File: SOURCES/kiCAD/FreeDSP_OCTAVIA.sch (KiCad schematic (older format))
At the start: 163 parts, among them IC1 TPS5430DDA, J13 Conn_01x05, J2 DC7.5V-9V IN, J4 Header_01x06, J7 Header_01x04, J8 Header_01x04, P1 Conn_02x20_Odd_Even, Q1 AO3401A, Q2 MMBT5401, Q3 2N7002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

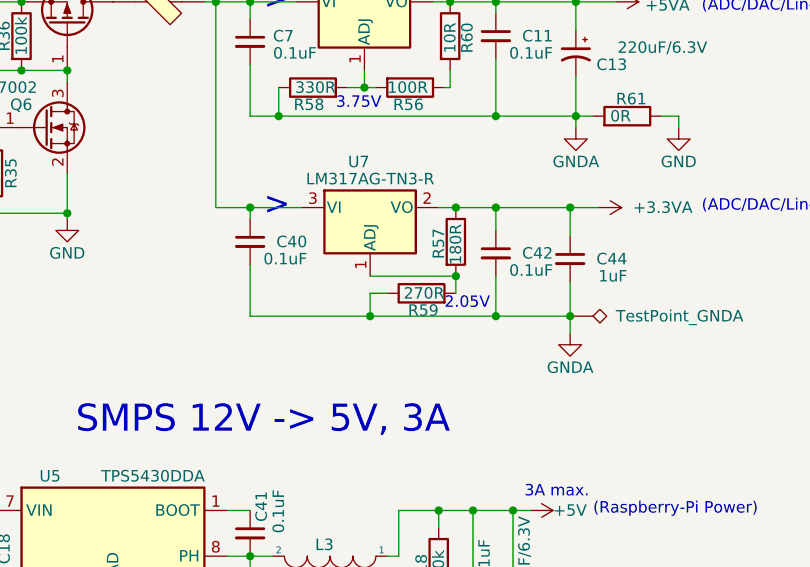
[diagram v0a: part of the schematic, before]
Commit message: Fixed R57, R59 value errors
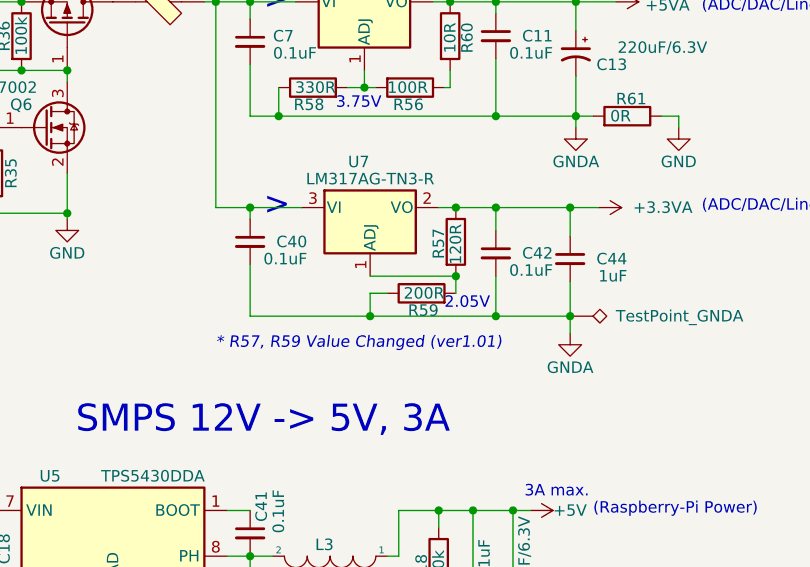
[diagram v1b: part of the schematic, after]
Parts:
- R57: value 180R -> 120R
- R59: value 270R -> 200R; JLPCB# C22962 -> C8218
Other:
- note added: "* R57, R59 Value Changed (ver1.01)"
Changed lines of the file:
@@
 Sheet 1 3
 Title "FreeDSP OVTAVIA Main Board"
-Date "2023-09-30"
-Rev "1.00"
+Date "2023-10-07"
+Rev "1.01"
 Comp ""
 Comment1 ""
@@
 P 10850 4450
 F 0 "R59" V 10775 4375 50  0000 L CNN
-F 1 "270R" V 10850 4350 50  0000 L CNN
+F 1 "200R" V 10850 4350 50  0000 L CNN
 F 2 "Resistor_SMD:R_0603_1608Metric" V 10780 4450 50  0001 C CNN
 F 3 "~" H 10850 4450 50  0001 C CNN
-F 4 "C22962" H 10850 4450 50  0001 C CNN "JLPCB#"
+F 4 "C8218" H 10850 4450 50  0001 C CNN "JLPCB#"
 	1    10850 4450
 	0    -1   -1   0
@@
 P 11000 4225
 F 0 "R57" V 10925 4150 50  0000 L CNN
-F 1 "180R" V 11000 4125 50  0000 L CNN
+F 1 "120R" V 11000 4125 50  0000 L CNN
 F 2 "Resistor_SMD:R_0603_1608Metric" V 10930 4225 50  0001 C CNN
 F 3 "~" H 11000 4225 50  0001 C CNN
@@
 Wire Wire Line
 	11975 3675 11900 3675
+Text Notes 9950 4700 0    50   Italic 0
+* R57, R59 Value Changed (ver1.01)
 $EndSCHEMATC

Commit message: Fixed ACM9070F Land Patterns.
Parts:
- FL1: footprint MyLibrary:ACM9070 -> MyLibrary:ACM9070F
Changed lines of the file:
@@
 Sheet 1 3
 Title "FreeDSP OVTAVIA Main Board"
-Date "2023-10-07"
-Rev "1.01"
+Date "2023-11-29"
+Rev "1.02"
 Comp ""
 Comment1 ""
@@
 F 0 "FL1" H 2650 1575 50  0000 C CNN
 F 1 "ACM9070" H 2725 1500 50  0000 C CNN
-F 2 "MyLibrary:ACM9070" V 2425 1365 50  0001 C CNN
+F 2 "MyLibrary:ACM9070F" V 2425 1365 50  0001 C CNN
 F 3 "~" V 2425 1365 50  0000 C CNN
 F 4 "C908578" H 2425 1325 50  0001 C CNN "JLPCB#"

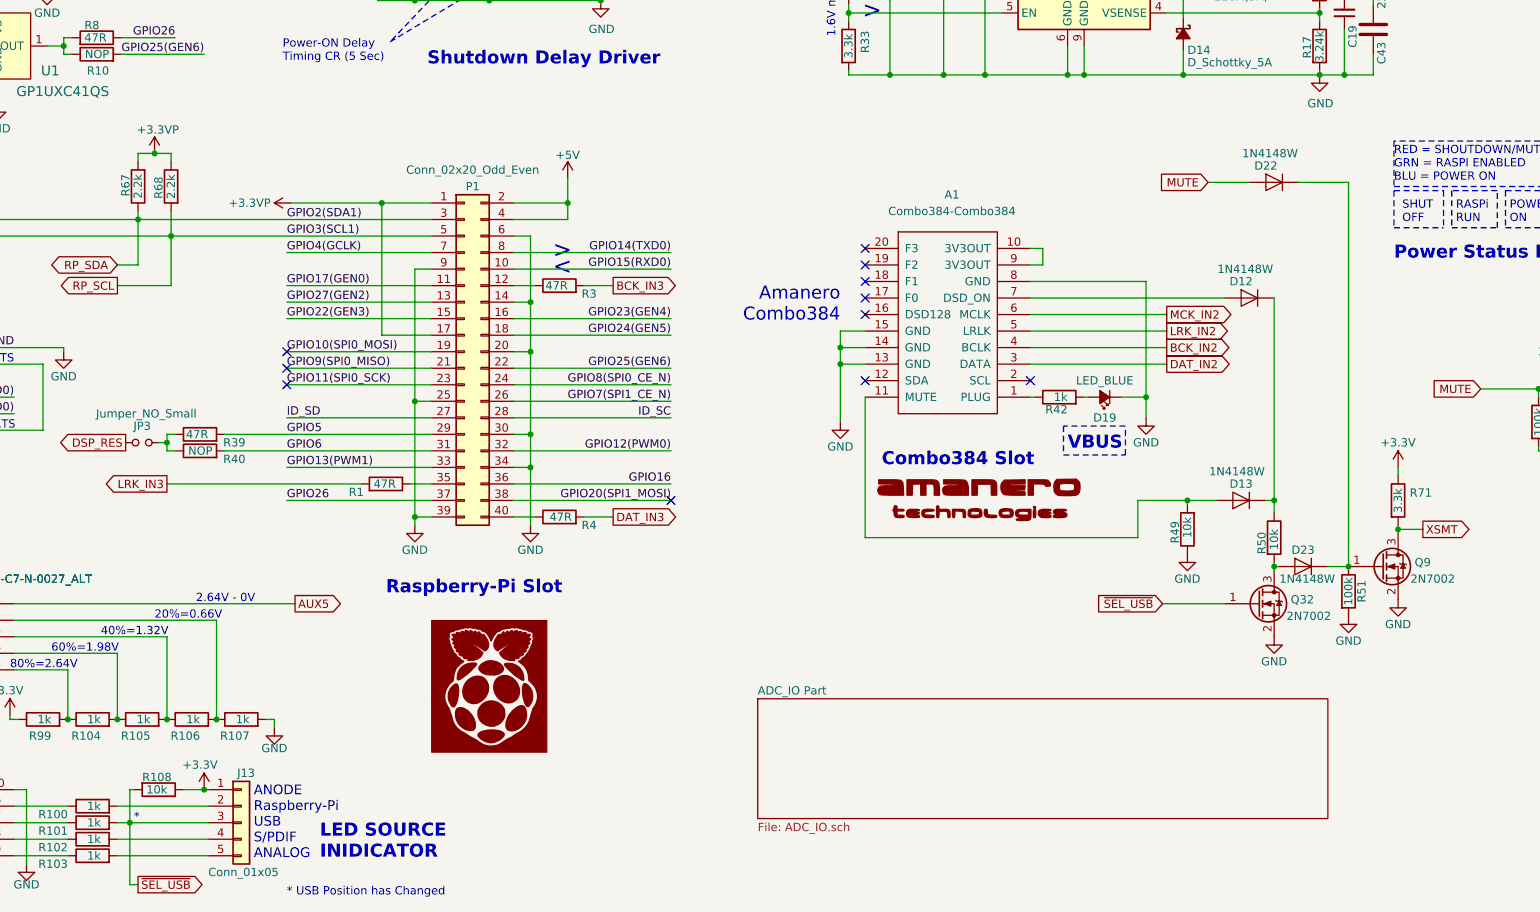
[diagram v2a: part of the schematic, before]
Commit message: Fixed ACM9070 lands. Selectable I2C for RPI/YORK
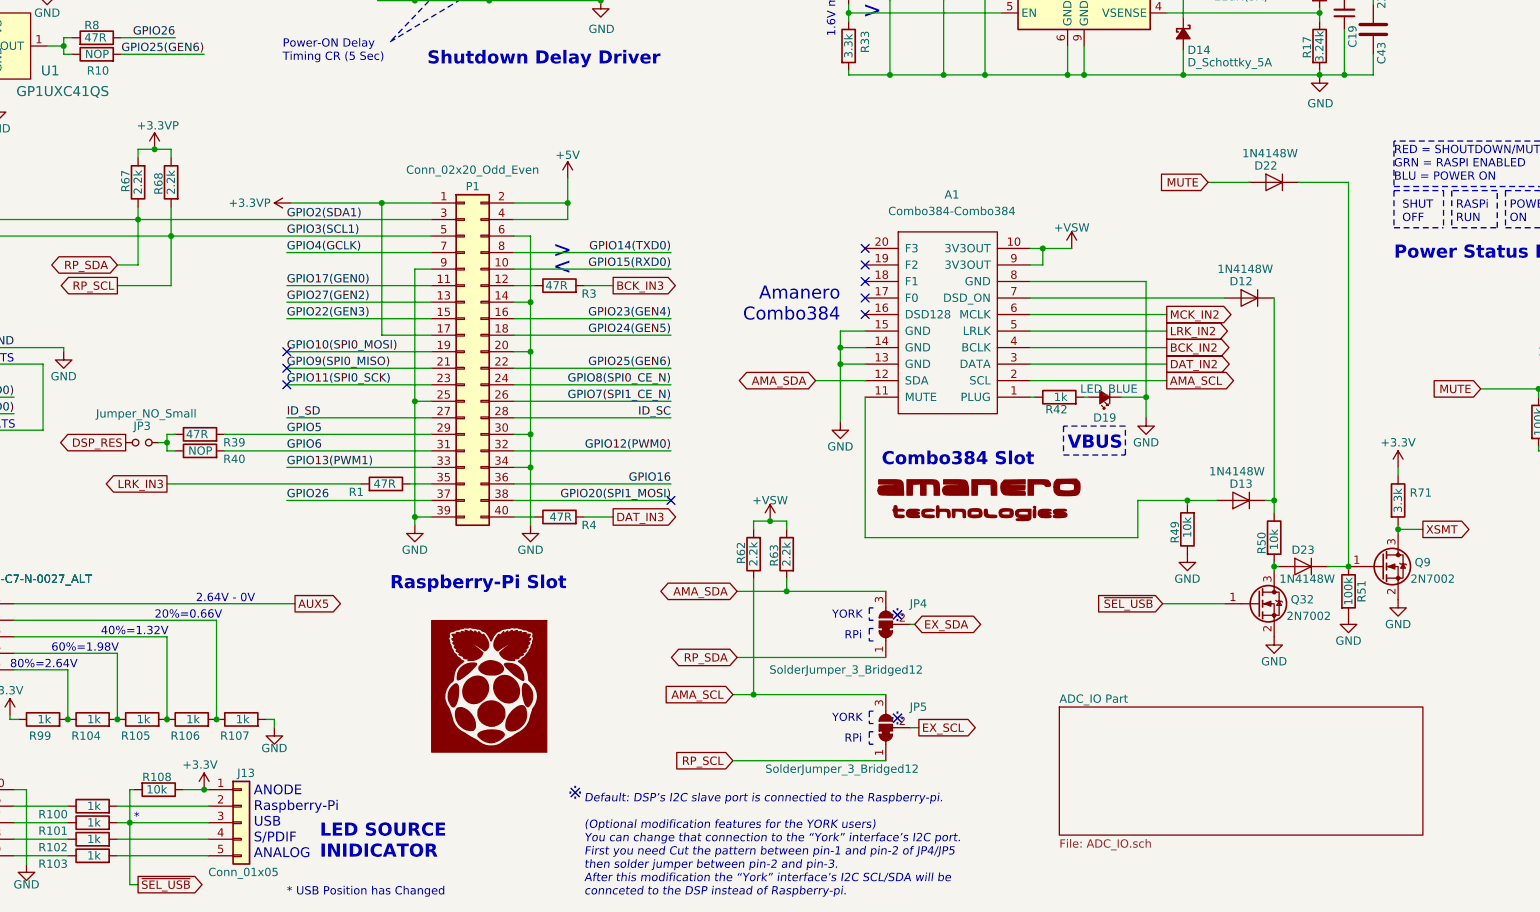
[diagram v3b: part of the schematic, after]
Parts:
- added JP4, JP5: SolderJumper_3_Bridged12, Jumper:SolderJumper-3_P1.3mm_Bridged12_Pad1.0x1.5mm_NumberLabels, symbol Jumper:SolderJumper_3_Bridged12
- added R62, R63: 2.2k, Resistor_SMD:R_0603_1608Metric, symbol Device:R
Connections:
- net RP_SCL: now also JP5.1 (A)
- net RP_SDA: now also JP4.1 (A)
- net +VSW: now reaches A1.10 (3V3OUT), A1.9 (3V3OUT)
- net +VSW: now also R62.2, R63.1
- net AMA_SDA: now reaches A1.12 (SDA)
- net AMA_SDA: now also JP4.3 (B), R63.2
- net AMA_SCL: now reaches A1.2 (SCL)
- net AMA_SCL: now also JP5.3 (B), R62.1
- new net EX_SCL: JP5.2 (C)
- new net EX_SDA: JP4.2 (C)
- no-connect marks 14 -> 12
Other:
- note added: "Default: DSP’s I2C slave port is connectied to the Raspberry-pi.\n\n(Optional modification features for the YORK users) \nYou can change that connection to the “York” interface’s I2C port.\nFirst you need Cut the pattern between pin-1 and pin-2 of JP4/JP5\nthen solder jumper between pin-2 and pin-3. \nAfter this modification the “York” interface’s I2C SCL/SDA will be \nconnceted to the DSP instea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"
- note added: "RPi"
- note added: "YORK"
- note added: "※"
- moved on the sheet: R67, R68
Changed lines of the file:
@@
 Sheet 1 3
 Title "FreeDSP OVTAVIA Main Board"
-Date "2023-11-29"
-Rev "1.02"
+Date "2023-12-03"
+Rev "1.1"
 Comp ""
 Comment1 ""
@@
 Wire Wire Line
 	10100 3175 10100 3250
-Text Notes 5275 9325 0    79   ~ 16
+Text Notes 5300 9300 0    79   ~ 16
 Raspberry-Pi Slot
 $Comp
@@
 RP_SDA
 $Comp
-L Device:R R67
-U 1 1 5E003EE5
-P 3775 6850
-F 0 "R67" V 3850 6775 50  0000 L CNN
-F 1 "2.2k" V 3775 6775 50  0000 L CNN
-F 2 "Resistor_SMD:R_0603_1608Metric" V 3705 6850 50  0001 C CNN
-F 3 "~" H 3775 6850 50  0001 C CNN
-F 4 "C4190" H 3775 6850 50  0001 C CNN "JLPCB#"
-	1    3775 6850
-	-1   0    0    1
-$EndComp
-$Comp
-L Device:R R68
-U 1 1 5E024BBA
-P 3975 6850
-F 0 "R68" V 4050 6775 50  0000 L CNN
-F 1 "2.2k" V 3975 6775 50  0000 L CNN
-F 2 "Resistor_SMD:R_0603_1608Metric" V 3905 6850 50  0001 C CNN
-F 3 "~" H 3975 6850 50  0001 C CNN
-F 4 "C4190" H 3975 6850 50  0001 C CNN "JLPCB#"
-	1    3975 6850
-	-1   0    0    -1
-$EndComp
-$Comp
 L Connector_Generic:Conn_01x04 J8
 U 1 1 5DB14FD9
@@
 $EndComp
 $Sheet
-S 7525 9950 3450 725
+S 9350 10000 2200 775
 U 5D902CF8
 F0 "ADC_IO Part" 50
@@
 NoConn ~ 8175 7525
 NoConn ~ 8175 7625
-NoConn ~ 9175 8025
-NoConn ~ 8175 8025
 $Comp
 L AmaneoLogo:LOGO Z?
@@
 AR Path="/651AEBA8" Ref="D19"  Part="1"
 F 0 "D19" H 9625 8250 50  0000 C CNN
-F 1 "LED_BLUE" H 9625 8025 50  0000 C CNN
+F 1 "LED_BLUE" H 9600 8075 50  0000 C CNN
 F 2 "LED_SMD:LED_0603_1608Metric_Castellated" V 9625 8125 60  0001 C CNN
 F 3 "" V 9625 8125 60  0000 C CNN
@@
 Wire Wire Line
 	7000 8050 6050 8050
-Wire Wire Line
-	3775 7000 3775 7050
 Connection ~ 3775 7050
 Wire Wire Line
 	3775 7050 5550 7050
-Wire Wire Line
-	3975 7000 3975 7150
 Connection ~ 3975 7150
 Wire Wire Line
 	3975 7150 5550 7150
 Wire Wire Line
-	3775 6700 3775 6650
-Wire Wire Line
-	3975 6650 3975 6700
-Wire Wire Line
 	3975 7450 3975 7150
 Wire Wire Line
@@
 Wire Wire Line
 	3775 7325 3775 7050
-$Comp
-L power:+3.3VP #PWR0204
-U 1 1 66B0497D
-P 3875 6650
-F 0 "#PWR0204" H 4025 6600 50  0001 C CNN
-F 1 "+3.3VP" H 3895 6793 50  0000 C CNN
-F 2 "" H 3875 6650 50  0001 C CNN
-F 3 "" H 3875 6650 50  0001 C CNN
-	1    3875 6650
-	1    0    0    -1
-$EndComp
-Wire Wire Line
-	3775 6650 3875 6650
-Connection ~ 3875 6650
-Wire Wire Line
-	3875 6650 3975 6650
 NoConn ~ 7000 8750
 NoConn ~ 4675 8050
@@
 Text Notes 9950 4700 0    50   Italic 0
 * R57, R59 Value Changed (ver1.01)
+Text GLabel 10000 8025 2    50   Output ~ 0
+AMA_SCL
+Wire Wire Line
+	9175 8025 10000 8025
+Text GLabel 7875 8025 0    50   BiDi ~ 0
+AMA_SDA
+Wire Wire Line
+	7875 8025 8175 8025
+Text GLabel 7400 9300 0    50   BiDi ~ 0
+AMA_SDA
+Text GLabel 7375 9925 0    50   Input ~ 0
+AMA_SCL
+Text GLabel 7400 9700 0    50   BiDi ~ 0
+RP_SDA
+Text GLabel 7375 10325 0    50   Input ~ 0
+RP_SCL
+$Comp
+L Jumper:SolderJumper_3_Bridged12 JP4
+U 1 1 65B1C7A7
+P 8300 9500
+F 0 "JP4" V 8425 9250 50  0000 L CNN
+F 1 "SolderJumper_3_Bridged12" V 8025 9275 50  0000 L CNN
+F 2 "Jumper:SolderJumper-3_P1.3mm_Bridged12_Pad1.0x1.5mm_NumberLabels" H 8300 9500 50  0001 C CNN
+F 3 "~" H 8300 9500 50  0001 C CNN
+	1    8300 9500
+	0    -1   -1   0
+$EndComp
+$Comp
+L Jumper:SolderJumper_3_Bridged12 JP5
+U 1 1 65B211AB
+P 8300 10125
+F 0 "JP5" V 8425 9875 50  0000 L CNN
+F 1 "SolderJumper_3_Bridged12" V 8050 9925 50  0000 L CNN
+F 2 "Jumper:SolderJumper-3_P1.3mm_Bridged12_Pad1.0x1.5mm_NumberLabels" H 8300 10125 50  0001 C CNN
+F 3 "~" H 8300 10125 50  0001 C CNN
+	1    8300 10125
+	0    -1   -1   0
+$EndComp
+Wire Wire Line
+	7400 9700 8300 9700
+Wire Wire Line
+	7375 10325 8300 10325
+Text GLabel 8475 9500 2    50   BiDi ~ 0
+EX_SDA
+Text GLabel 8500 10125 2    50   Output ~ 0
+EX_SCL
+Wire Wire Line
+	3875 6625 3975 6625
+Wire Wire Line
+	3775 6625 3875 6625
+Connection ~ 3875 6625
+$Comp
+L power:+3.3VP #PWR0204
+U 1 1 66B0497D
+P 3875 6625
+F 0 "#PWR0204" H 4025 6575 50  0001 C CNN
+F 1 "+3.3VP" H 3895 6768 50  0000 C CNN
+F 2 "" H 3875 6625 50  0001 C CNN
+F 3 "" H 3875 6625 50  0001 C CNN
+	1    3875 6625
+	1    0    0    -1
+$EndComp
+Wire Wire Line
+	3975 6625 3975 6675
+Wire Wire Line
+	3775 6675 3775 6625
+$Comp
+L Device:R R68
+U 1 1 5E024BBA
+P 3975 6825
+F 0 "R68" V 4050 6750 50  0000 L CNN
+F 1 "2.2k" V 3975 6750 50  0000 L CNN
+F 2 "Resistor_SMD:R_0603_1608Metric" V 3905 6825 50  0001 C CNN
+F 3 "~" H 3975 6825 50  0001 C CNN
+F 4 "C4190" H 3975 6825 50  0001 C CNN "JLPCB#"
+	1    3975 6825
+	-1   0    0    -1
+$EndComp
+$Comp
+L Device:R R67
+U 1 1 5E003EE5
+P 3775 6825
+F 0 "R67" V 3850 6750 50  0000 L CNN
+F 1 "2.2k" V 3775 6750 50  0000 L CNN
+F 2 "Resistor_SMD:R_0603_1608Metric" V 3705 6825 50  0001 C CNN
+F 3 "~" H 3775 6825 50  0001 C CNN
+F 4 "C4190" H 3775 6825 50  0001 C CNN "JLPCB#"
+	1    3775 6825
+	-1   0    0    1
+$EndComp
+Wire Wire Line
+	3775 6975 3775 7050
+Wire Wire Line
+	3975 6975 3975 7150
+Wire Wire Line
+	7700 8875 7700 8925
+Wire Wire Line
+	7500 8925 7500 8875
+$Comp
+L Device:R R63
+U 1 1 65B96867
+P 7700 9075
+F 0 "R63" V 7775 9000 50  0000 L CNN
+F 1 "2.2k" V 7700 9000 50  0000 L CNN
+F 2 "Resistor_SMD:R_0603_1608Metric" V 7630 9075 50  0001 C CNN
+F 3 "~" H 7700 9075 50  0001 C CNN
+F 4 "C4190" H 7700 9075 50  0001 C CNN "JLPCB#"
+	1    7700 9075
+	-1   0    0    -1
+$EndComp
+$Comp
+L Device:R R62
+U 1 1 65B9686E
+P 7500 9075
+F 0 "R62" V 7575 9000 50  0000 L CNN
+F 1 "2.2k" V 7500 9000 50  0000 L CNN
+F 2 "Resistor_SMD:R_0603_1608Metric" V 7430 9075 50  0001 C CNN
+F 3 "~" H 7500 9075 50  0001 C CNN
+F 4 "C4190" H 7500 9075 50  0001 C CNN "JLPCB#"
+	1    7500 9075
+	-1   0    0    1
+$EndComp
+Wire Wire Line
+	8450 9500 8475 9500
+Wire Wire Line
+	8450 10125 8500 10125
+Wire Wire Line
+	7375 9925 7500 9925
+Wire Wire Line
+	7400 9300 7700 9300
+Wire Wire Line
+	7500 9225 7500 9925
+Connection ~ 7500 9925
+Wire Wire Line
+	7500 9925 8300 9925
+Wire Wire Line
+	7700 9225 7700 9300
+Connection ~ 7700 9300
+Wire Wire Line
+	7700 9300 8300 9300
+Wire Wire Line
+	9250 7225 9425 7225
+Connection ~ 9250 7225
+$Comp
+L power:+VSW #PWR0154
+U 1 1 6604037A
+P 7600 8875
+F 0 "#PWR0154" H 7600 8725 50  0001 C CNN
+F 1 "+VSW" H 7600 9000 50  0000 C CNN
+F 2 "" H 7600 8875 50  0001 C CNN
+F 3 "" H 7600 8875 50  0001 C CNN
+	1    7600 8875
+	1    0    0    -1
+$EndComp
+$Comp
+L power:+VSW #PWR0155
+U 1 1 66043AE6
+P 9425 7225
+F 0 "#PWR0155" H 9425 7075 50  0001 C CNN
+F 1 "+VSW" H 9425 7350 50  0000 C CNN
+F 2 "" H 9425 7225 50  0001 C CNN
+F 3 "" H 9425 7225 50  0001 C CNN
+	1    9425 7225
+	1    0    0    -1
+$EndComp
+Wire Wire Line
+	7500 8875 7600 8875
+Connection ~ 7600 8875
+Wire Wire Line
+	7600 8875 7700 8875
+Text Notes 6475 11150 0    50   Italic 0
+Default: DSP’s I2C slave port is connectied to the Raspberry-pi.\n\n(Optional modification features for the YORK users)  \nYou can change that connection to the “York” interface’s I2C port.\nFirst you need Cut the pattern between pin-1 and pin-2 of JP4/JP5\nthen solder jumper between pin-2 and pin-3. \nAfter this modification the “York” interface’s I2C SCL/SDA will be \nconnceted to the DSP instead of Raspberry-pi.
+Text Notes 6375 10575 0    79   ~ 0
+※
+Text Notes 8325 9500 0    79   ~ 0
+※
+Text Notes 8325 10125 0    79   ~ 0
+※
+Wire Notes Line style solid
+	8225 9400 8200 9400
+Wire Notes Line style solid
+	8200 9400 8200 9475
+Wire Notes Line style solid
+	8200 9475 8225 9475
+Wire Notes Line style solid
+	8225 9525 8200 9525
+Wire Notes Line style solid
+	8200 9525 8200 9600
+Wire Notes Line style solid
+	8200 9600 8225 9600
+Text Notes 7975 9475 0    49   ~ 0
+YORK
+Text Notes 8050 9600 0    49   ~ 0
+RPi
+Wire Notes Line style solid
+	8225 10025 8200 10025
+Wire Notes Line style solid
+	8200 10025 8200 10100
+Wire Notes Line style solid
+	8200 10100 8225 10100
+Wire Notes Line style solid
+	8225 10150 8200 10150
+Wire Notes Line style solid
+	8200 10150 8200 10225
+Wire Notes Line style solid
+	8200 10225 8225 10225
+Text Notes 7975 10100 0    49   ~ 0
+YORK
+Text Notes 8050 10225 0    49   ~ 0
+RPi
 $EndSCHEMATC
